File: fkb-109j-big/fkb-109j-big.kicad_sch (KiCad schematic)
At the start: 279 parts

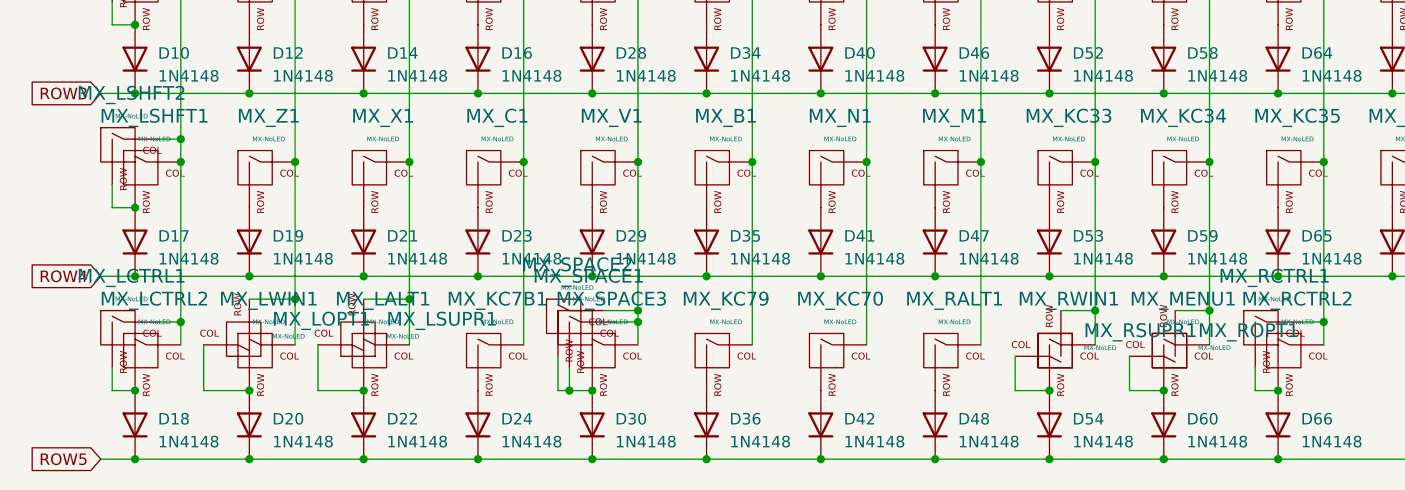
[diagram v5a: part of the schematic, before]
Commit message: add 7u/jis bottom-row
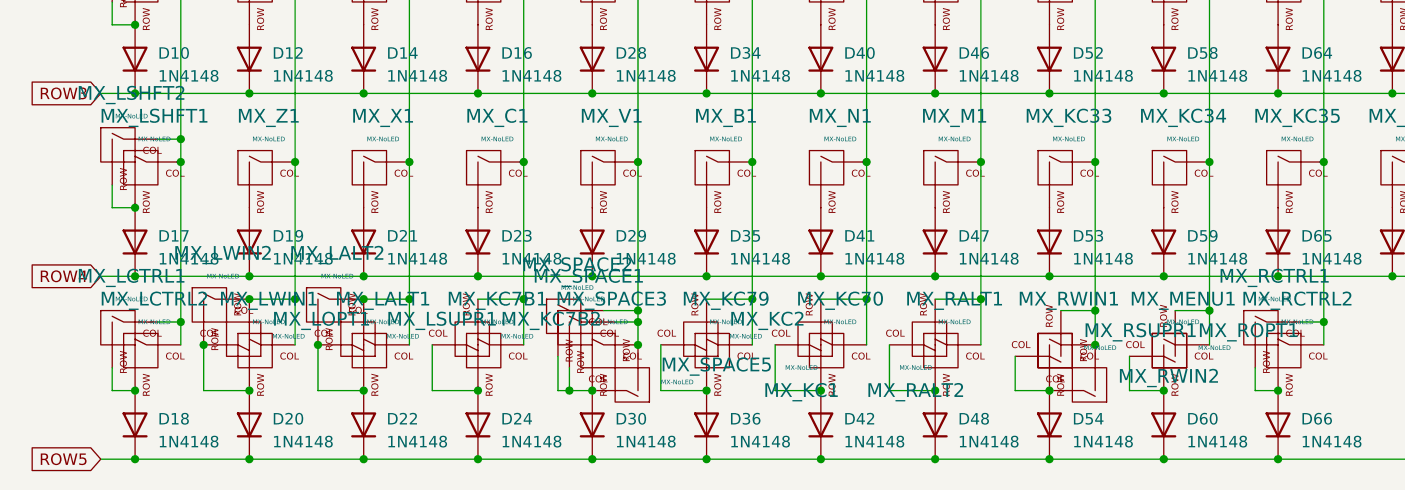
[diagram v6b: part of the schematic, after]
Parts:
- added MX_KC1, MX_LALT2, MX_RALT2: MX-NoLED, Alps_Only:ALPS-1.5U, symbol MX_Alps_Hybrid:MX-NoLED
- added MX_KC2, MX_KC7B2: MX-NoLED, Alps_Only:ALPS-1.75U, symbol MX_Alps_Hybrid:MX-NoLED
- added MX_LWIN2, MX_RWIN2: MX-NoLED, Alps_Only:ALPS-1U, symbol MX_Alps_Hybrid:MX-NoLED
- added MX_SPACE5: MX-NoLED, Alps_Only:ALPS-2U, symbol MX_Alps_Hybrid:MX-NoLED
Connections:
- net COL1: now also MX_LWIN2.1 (COL)
- net COL2: now also MX_LALT2.1 (COL)
- net COL3: now also MX_KC7B2.2 (ROW)
- net COL4: now also MX_SPACE5.2 (ROW)
- net COL5: now also MX_KC2.2 (ROW)
- net COL6: now also MX_KC1.2 (ROW)
- net COL7: now also MX_RALT2.2 (ROW)
- net COL8: now also MX_RWIN2.2 (ROW)
- net at D24.2 (A), MX_KC7B1.2 (ROW): now also MX_KC7B2.1 (COL)
- net at D30.2 (A), MX_SPACE1.2 (ROW), MX_SPACE2.2 (ROW)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: now also MX_SPACE5.1 (COL)
- net at D36.2 (A), MX_KC79.2 (ROW): now also MX_KC2.1 (COL)
- net at D22.2 (A), MX_LALT1.2 (ROW), MX_LSUPR1.1 (COL): now also MX_LALT2.2 (ROW)
- net at D20.2 (A), MX_LOPT1.1 (COL), MX_LWIN1.2 (ROW): now also MX_LWIN2.2 (ROW)
- net at D54.2 (A), MX_RSUPR1.1 (COL), MX_RWIN1.2 (ROW): now also MX_RWIN2.1 (COL)
- net at D42.2 (A), MX_KC70.2 (ROW): now also MX_KC1.1 (COL)
- net at D48.2 (A), MX_RALT1.2 (ROW): now also MX_RALT2.1 (COL)

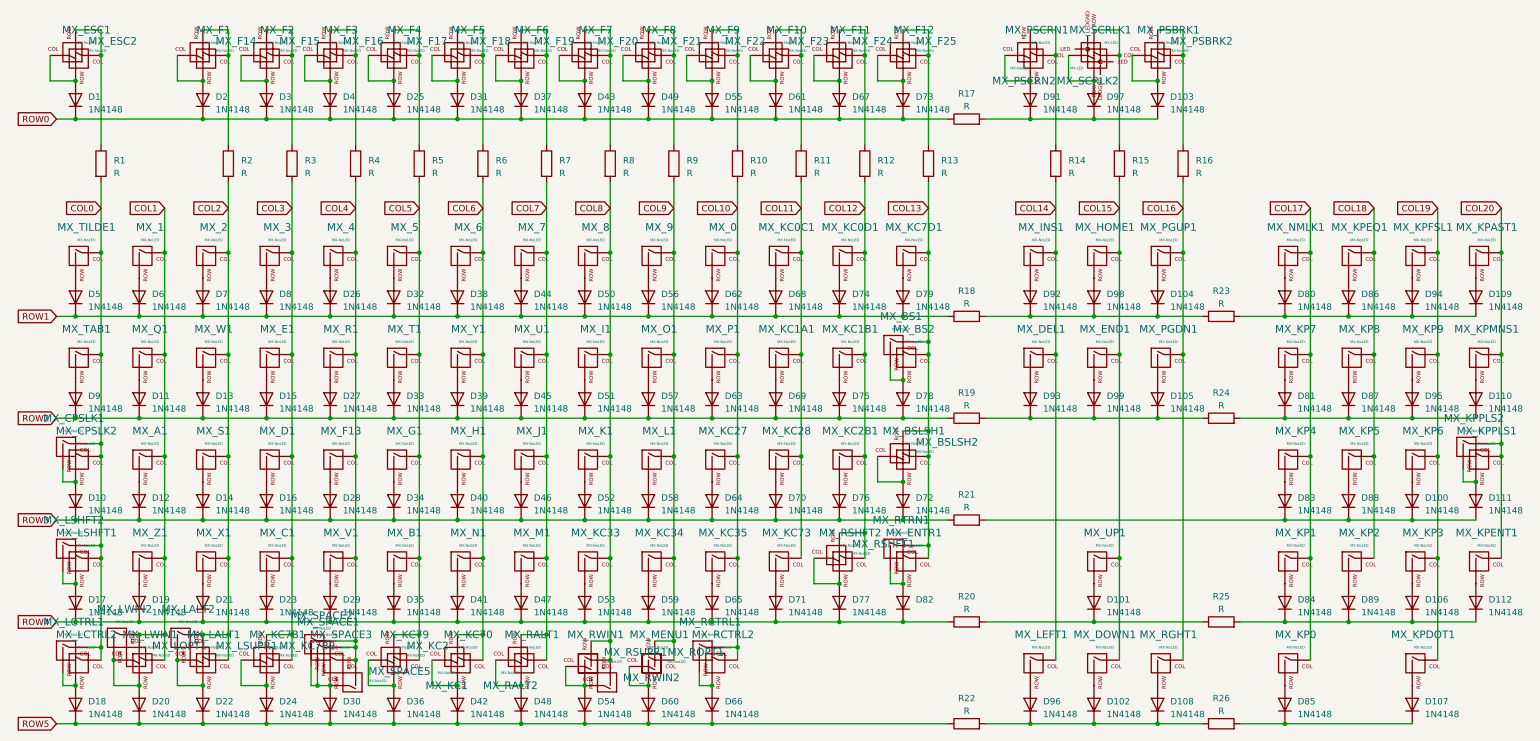
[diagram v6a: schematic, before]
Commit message: continue placing diodes
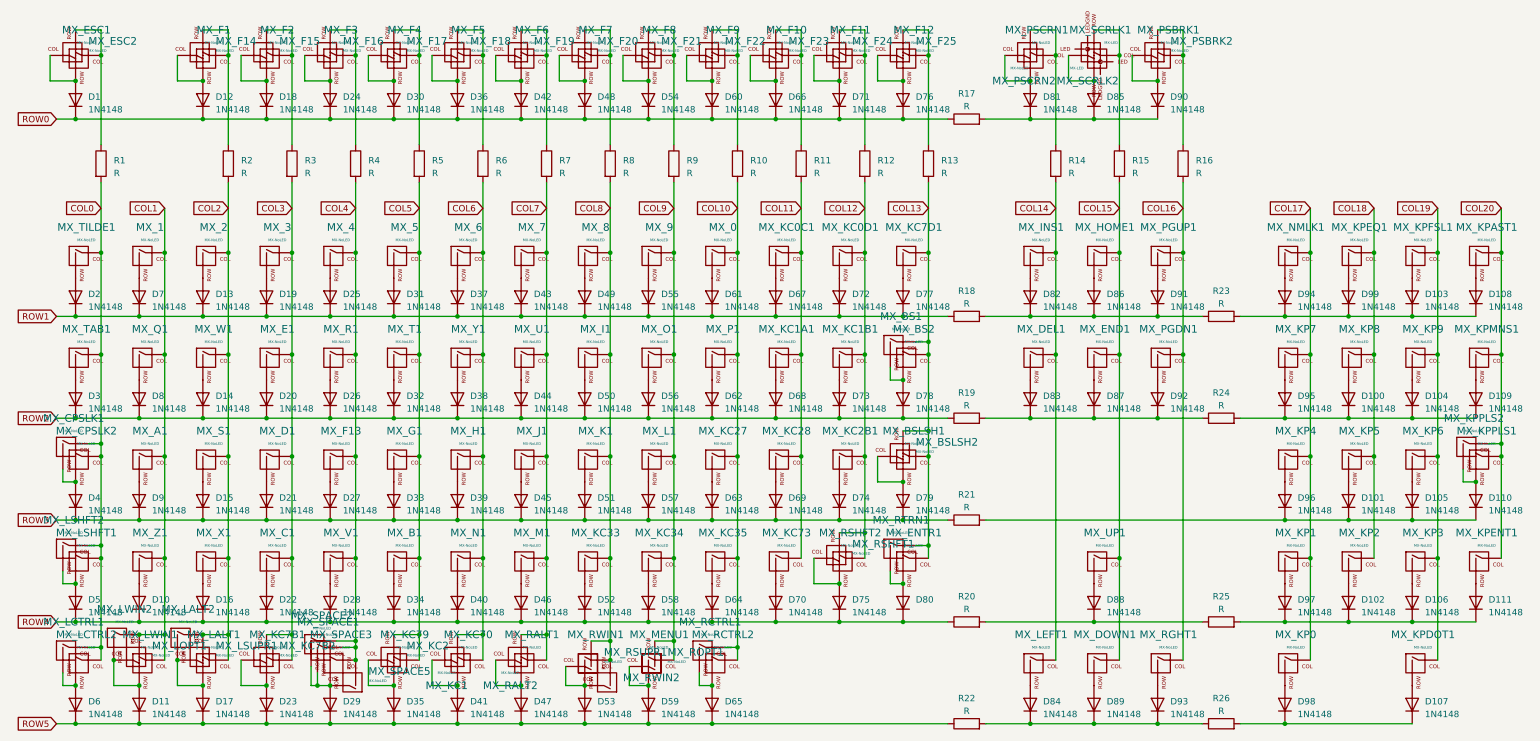
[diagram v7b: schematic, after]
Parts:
- renumbered D19 to D10, D87 to D100, D88 to D101, D89 to D102, D94 to D103, D95 to D104, D100 to D105, D109 to D108, D110 to D109, D20 to D11, D111 to D110, D112 to D111, D2 to D12, D7 to D13, D13 to D14, D14 to D15, D21 to D16, D22 to D17, D3 to D18, D8 to D19, D5 to D2, D15 to D20, D16 to D21, D23 to D22, D24 to D23, D4 to D24, D26 to D25, D27 to D26, D28 to D27, D29 to D28, D30 to D29, D9 to D3, D25 to D30, D32 to D31, D33 to D32, D34 to D33, D35 to D34, D36 to D35, D31 to D36, D38 to D37, D39 to D38, D40 to D39, D10 to D4, D41 to D40, D42 to D41, D37 to D42, D44 to D43, D45 to D44, D46 to D45, D47 to D46, D48 to D47, D43 to D48, D50 to D49, D17 to D5, D51 to D50, D52 to D51, D53 to D52, D54 to D53, D49 to D54, D56 to D55, D57 to D56, D58 to D57, D59 to D58, D60 to D59, D18 to D6, D55 to D60, D62 to D61, D63 to D62, D64 to D63, D65 to D64, D66 to D65, D61 to D66, D68 to D67, D69 to D68, D70 to D69, D6 to D7, D71 to D70, D67 to D71, D74 to D72, D75 to D73, D76 to D74, D77 to D75, D73 to D76, D79 to D77, D72 to D79, D11 to D8, D82 to D80, D91 to D81, D92 to D82, D93 to D83, D96 to D84, D97 to D85, D98 to D86, D99 to D87, D101 to D88, D102 to D89, D12 to D9, D103 to D90, D104 to D91, D105 to D92, D108 to D93, D80 to D94, D81 to D95, D83 to D96, D84 to D97, D85 to D98, D86 to D99

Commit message: layout cont.
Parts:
- removed R1, R10, R11, R12, R13, R17, R18, R19, R2, R20, R21, R22, R3, R4, R5, R6, R7, R8, R9: R, Resistor_THT:R_Axial_DIN0207_L6.3mm_D2.5mm_P10.16mm_Horizontal, symbol Device:R
- added J1, J2: Conn_02x07_Counter_Clockwise, Connector_PinHeader_2.00mm:PinHeader_1x14_P2.00mm_Vertical, symbol Connector_Generic:Conn_02x07_Counter_Clockwise
- added J3, J4: Conn_01x01_Pin, Connector_PinHeader_2.00mm:PinHeader_1x01_P2.00mm_Vertical, symbol Connector:Conn_01x01_Pin
- added J5: Conn_01x05_Pin, Connector_PinHeader_2.00mm:PinHeader_1x05_P2.00mm_Vertical, symbol Connector:Conn_01x05_Pin
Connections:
- net ROW1: now also J5.1 (Pin_1)
- net ROW2: now also J5.2 (Pin_2)
- net ROW3: now also J5.3 (Pin_3)
- net ROW4: now also J5.4 (Pin_4)
- net ROW5: now also J5.5 (Pin_5)
- net at D81.1 (K), D85.1 (K), D90.1 (K): now also J4.1 (Pin_1)
- net COL7_TOP: now reaches MX_F19.2 (ROW), MX_F6.1 (COL)
- net COL7_TOP: now also J2.8 (Pin_8)
- net COL12_TOP: now reaches MX_F11.1 (COL), MX_F24.2 (ROW)
- net COL12_TOP: now also J2.13 (Pin_13)
- net COL13_TOP: now reaches MX_F12.1 (COL), MX_F25.2 (ROW)
- net COL13_TOP: now also J2.14 (Pin_14)
- net COL8_TOP: now reaches MX_F20.2 (ROW), MX_F7.1 (COL)
- net COL8_TOP: now also J2.9 (Pin_9)
- net COL10_TOP: now reaches MX_F22.2 (ROW), MX_F9.1 (COL)
- net COL10_TOP: now also J2.11 (Pin_11)
- net COL11_TOP: now reaches MX_F10.1 (COL), MX_F23.2 (ROW)
- net COL11_TOP: now also J2.12 (Pin_12)
- net COL5_TOP: now reaches MX_F17.2 (ROW), MX_F4.1 (COL)
- net COL5_TOP: now also J2.6 (Pin_6)
- net COL3_TOP: now reaches MX_F15.2 (ROW), MX_F2.1 (COL)
- net COL3_TOP: now also J2.4 (Pin_4)
- net COL2_TOP: now reaches MX_F1.1 (COL), MX_F14.2 (ROW)
- net COL2_TOP: now also J2.3 (Pin_3)
- net COL6_TOP: now reaches MX_F18.2 (ROW), MX_F5.1 (COL)
- net COL6_TOP: now also J2.7 (Pin_7)
- net COL9_TOP: now reaches MX_F21.2 (ROW), MX_F8.1 (COL)
- net COL9_TOP: now also J2.10 (Pin_10)
- net COL0_TOP: now reaches MX_ESC1.1 (COL), MX_ESC2.2 (ROW)
- net COL0_TOP: now also J2.1 (Pin_1)
- net COL4_TOP: now reaches MX_F16.2 (ROW), MX_F3.1 (COL)
- net COL4_TOP: now also J2.5 (Pin_5)
- net COL0 renamed COL0_BOTTOM
- net COL0_BOTTOM: now also J1.1 (Pin_1)
- net COL1 renamed COL1_BOTTOM
- net COL1_BOTTOM: now also J1.2 (Pin_2)
- net COL10 renamed COL10_BOTTOM
- net COL10_BOTTOM: now also J1.11 (Pin_11)
- net COL11 renamed COL11_BOTTOM
- net COL11_BOTTOM: now also J1.12 (Pin_12)
- net COL12 renamed COL12_BOTTOM
- net COL12_BOTTOM: now also J1.13 (Pin_13)
- net COL13 renamed COL13_BOTTOM
- net COL13_BOTTOM: now also J1.14 (Pin_14)
- net COL14 renamed COL14_BOTTOM
- net COL15 renamed COL15_BOTTOM
- net COL16 renamed COL16_BOTTOM
- net COL17 renamed COL17_BOTTOM
- net COL18 renamed COL18_BOTTOM
- net COL19 renamed COL19_BOTTOM
- net COL2 renamed COL2_BOTTOM
- net COL2_BOTTOM: now also J1.3 (Pin_3)
- net COL20 renamed COL20_BOTTOM
- net COL3 renamed COL3_BOTTOM
- net COL3_BOTTOM: now also J1.4 (Pin_4)
- net COL4 renamed COL4_BOTTOM
- net COL4_BOTTOM: now also J1.5 (Pin_5)
- net COL5 renamed COL5_BOTTOM
- net COL5_BOTTOM: now also J1.6 (Pin_6)
- net COL6 renamed COL6_BOTTOM
- net COL6_BOTTOM: now also J1.7 (Pin_7)
- net COL7 renamed COL7_BOTTOM
- net COL7_BOTTOM: now also J1.8 (Pin_8)
- net COL8 renamed COL8_BOTTOM
- net COL8_BOTTOM: now also J1.9 (Pin_9)
- net COL9 renamed COL9_BOTTOM
- net COL9_BOTTOM: now also J1.10 (Pin_10)
- net ROW0 renamed ROW0_LEFT
- net ROW0_LEFT: now also J3.1 (Pin_1)
- new net COL1_TOP: J2.2 (Pin_2)
